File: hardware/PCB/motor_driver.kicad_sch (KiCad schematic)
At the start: 27 parts, among them U2 TMC2209-LA, U3 TB6612FNG, U4 TB6612FNG

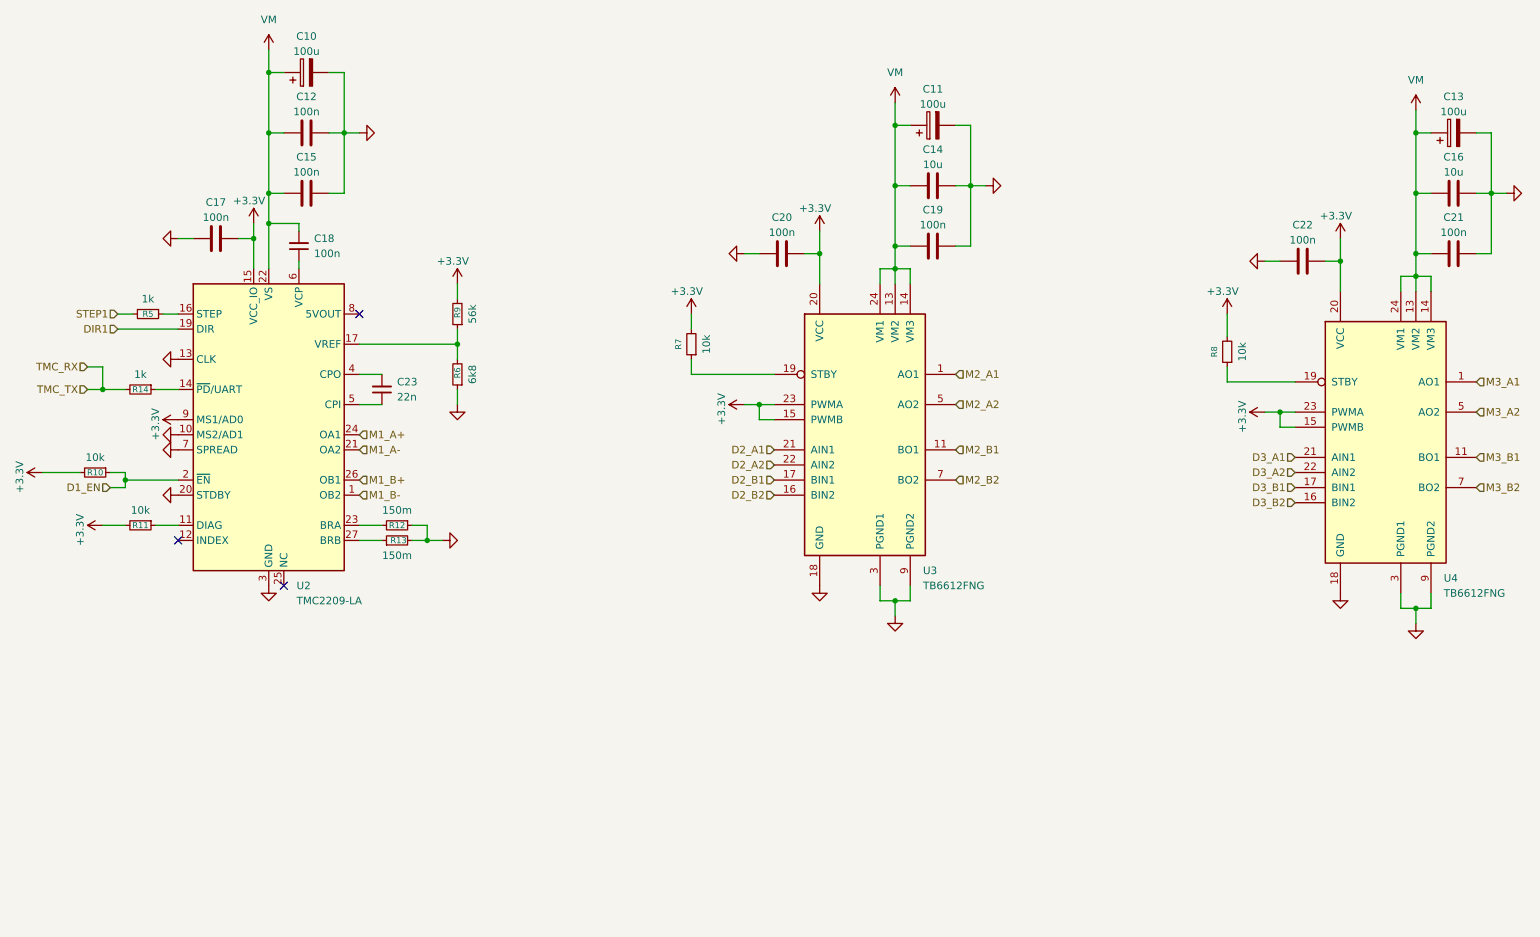
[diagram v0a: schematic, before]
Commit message: Added I2C expander for motor drivers and changed LoRa module
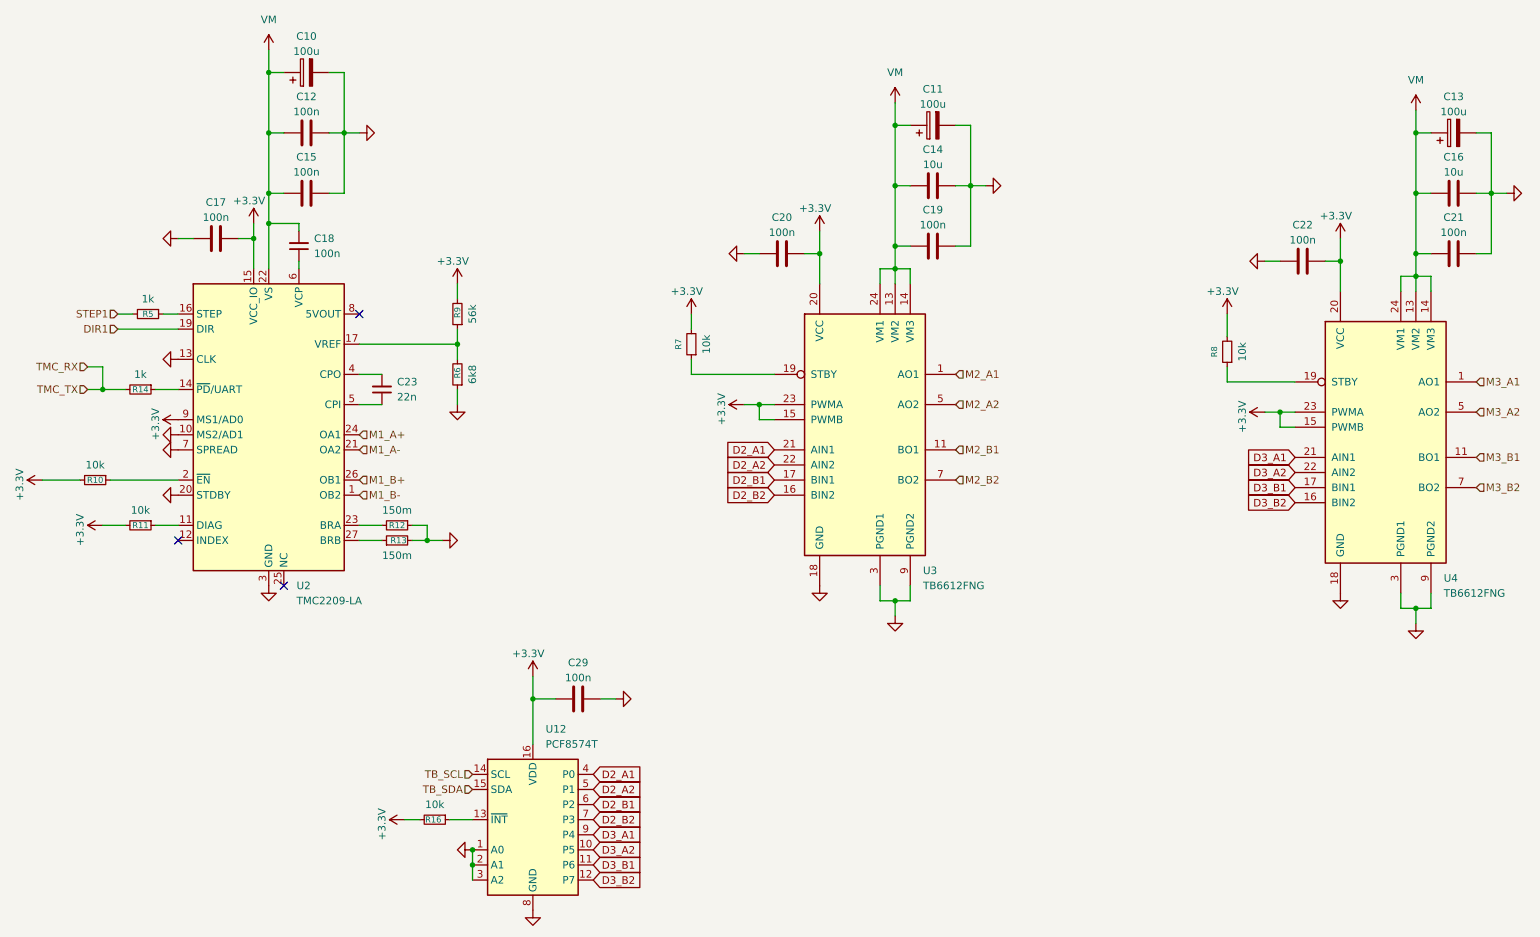
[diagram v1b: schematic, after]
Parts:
- added C29: 100n, Capacitor_SMD:C_1206_3216Metric_Pad1.33x1.80mm_HandSolder, symbol Device:C
- added R16: 10k, Resistor_SMD:R_1206_3216Metric_Pad1.30x1.75mm_HandSolder, symbol Device:R_Small
- added U12: PCF8574T, Package_SO:SOIC-16W_7.5x10.3mm_P1.27mm, symbol Interface_Expansion:PCF8574T
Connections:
- net +3.3V: now also C29.1, R16.2, U12.16 (VDD)
- net D2_A1: now also U12.4 (P0)
- net D2_A2: now also U12.5 (P1)
- net D2_B1: now also U12.6 (P2)
- net D2_B2: now also U12.7 (P3)
- net D3_A1: now also U12.9 (P4)
- net D3_A2: now also U12.10 (P5)
- net D3_B1: now also U12.11 (P6)
- net D3_B2: now also U12.12 (P7)
- net GND: now also C29.2, U12.1 (A0), U12.2 (A1), U12.3 (A2), U12.8 (GND)
- net D1_EN: no longer names the net of R10.1, U2.2 (~{EN})
- new net: R16.1, U12.13 (~{INT})
- new net TB_SCL: U12.14 (SCL)
- new net TB_SDA: U12.15 (SDA)
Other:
- moved on the sheet: R10

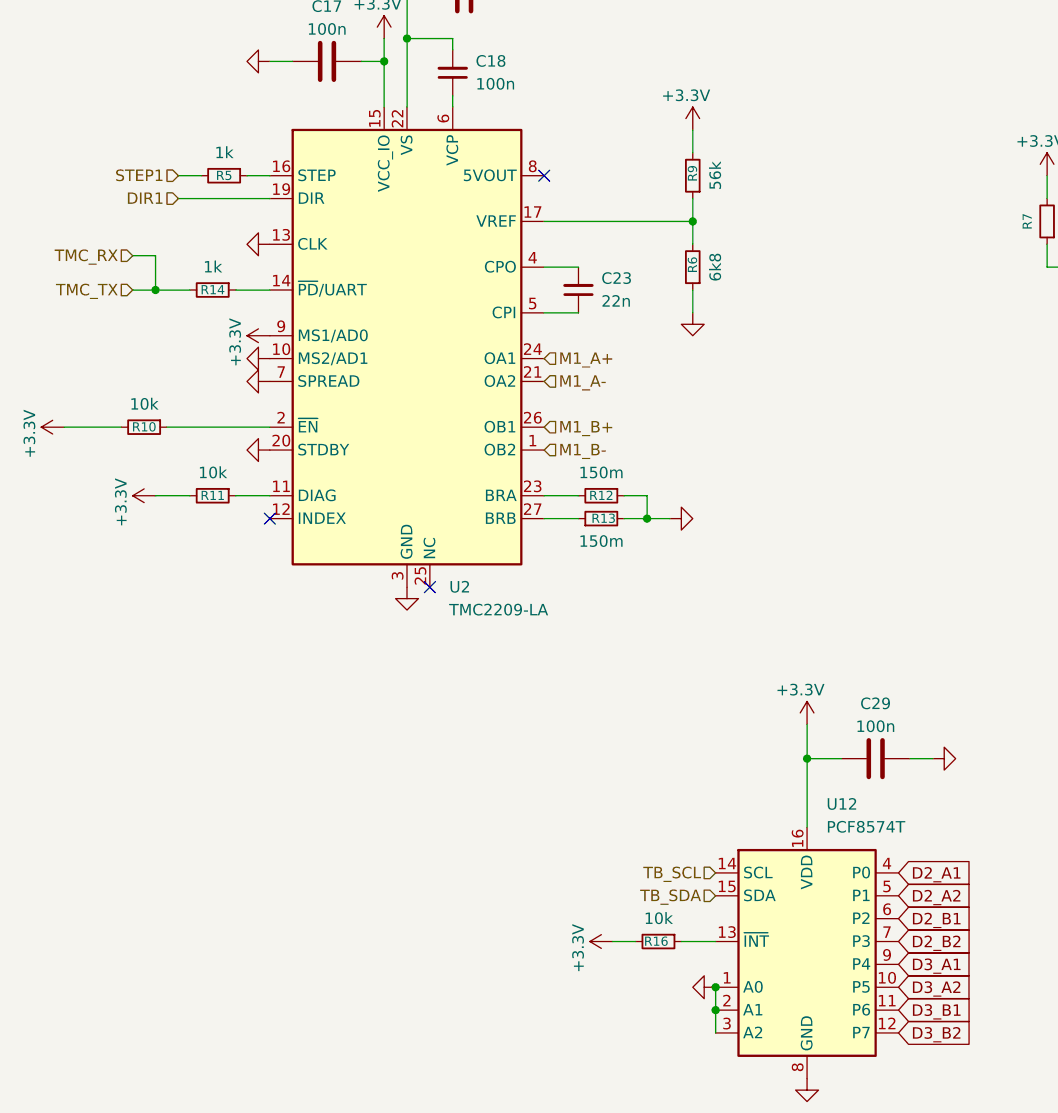
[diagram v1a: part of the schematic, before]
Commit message: Finished schematic for LoRa, added BME280
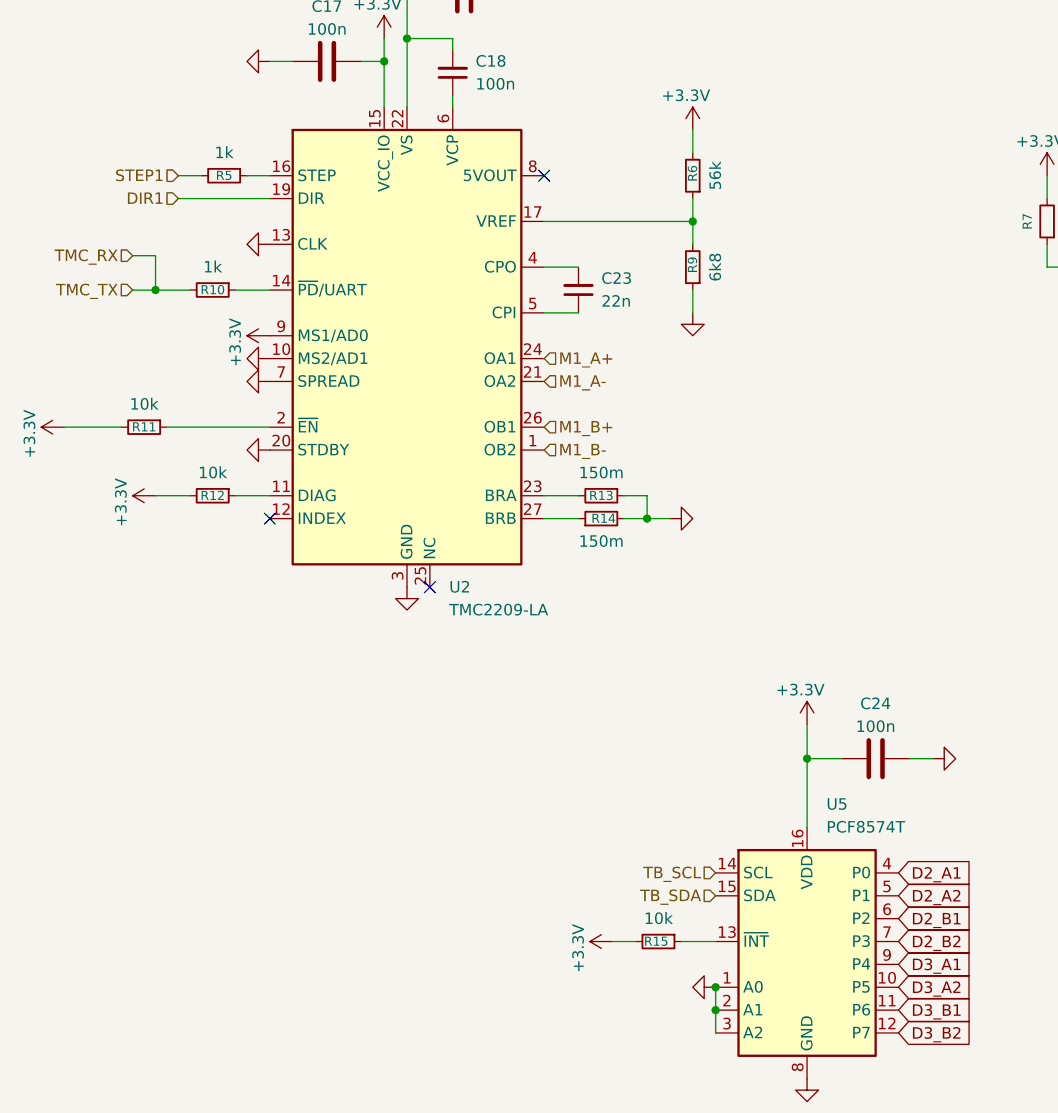
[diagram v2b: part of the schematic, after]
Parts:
- renumbered C29 to C24, R14 to R10, R10 to R11, R11 to R12, R12 to R13, R13 to R14, R16 to R15, R9 to R6, R6 to R9, U12 to U5

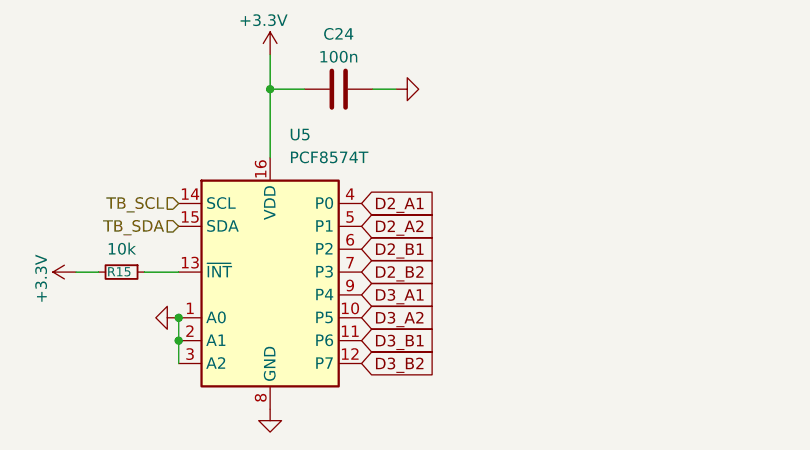
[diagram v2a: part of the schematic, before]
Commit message: Rerouted changes on the PCB layout, Routed LoRa
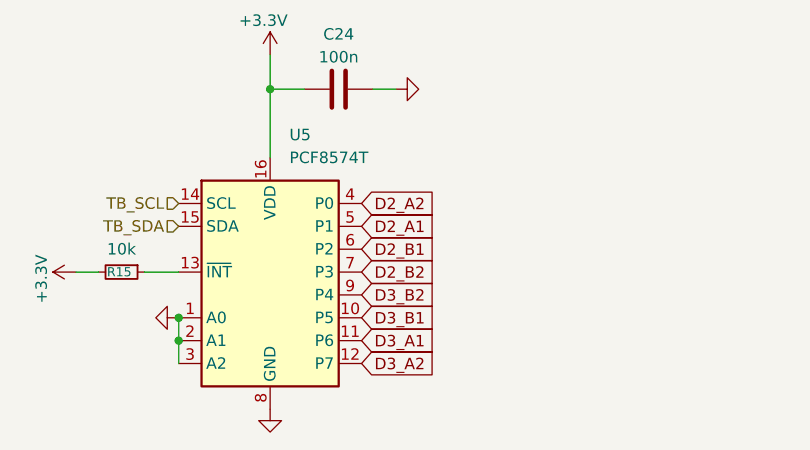
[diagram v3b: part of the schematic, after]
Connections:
- net D2_A1: now also U5.5 (P1); no longer U5.4 (P0)
- net D2_A2: now also U5.4 (P0); no longer U5.5 (P1)
- net D3_A1: now also U5.11 (P6); no longer U5.9 (P4)
- net D3_A2: now also U5.12 (P7); no longer U5.10 (P5)
- net D3_B1: now also U5.10 (P5); no longer U5.11 (P6)
- net D3_B2: now also U5.9 (P4); no longer U5.12 (P7)

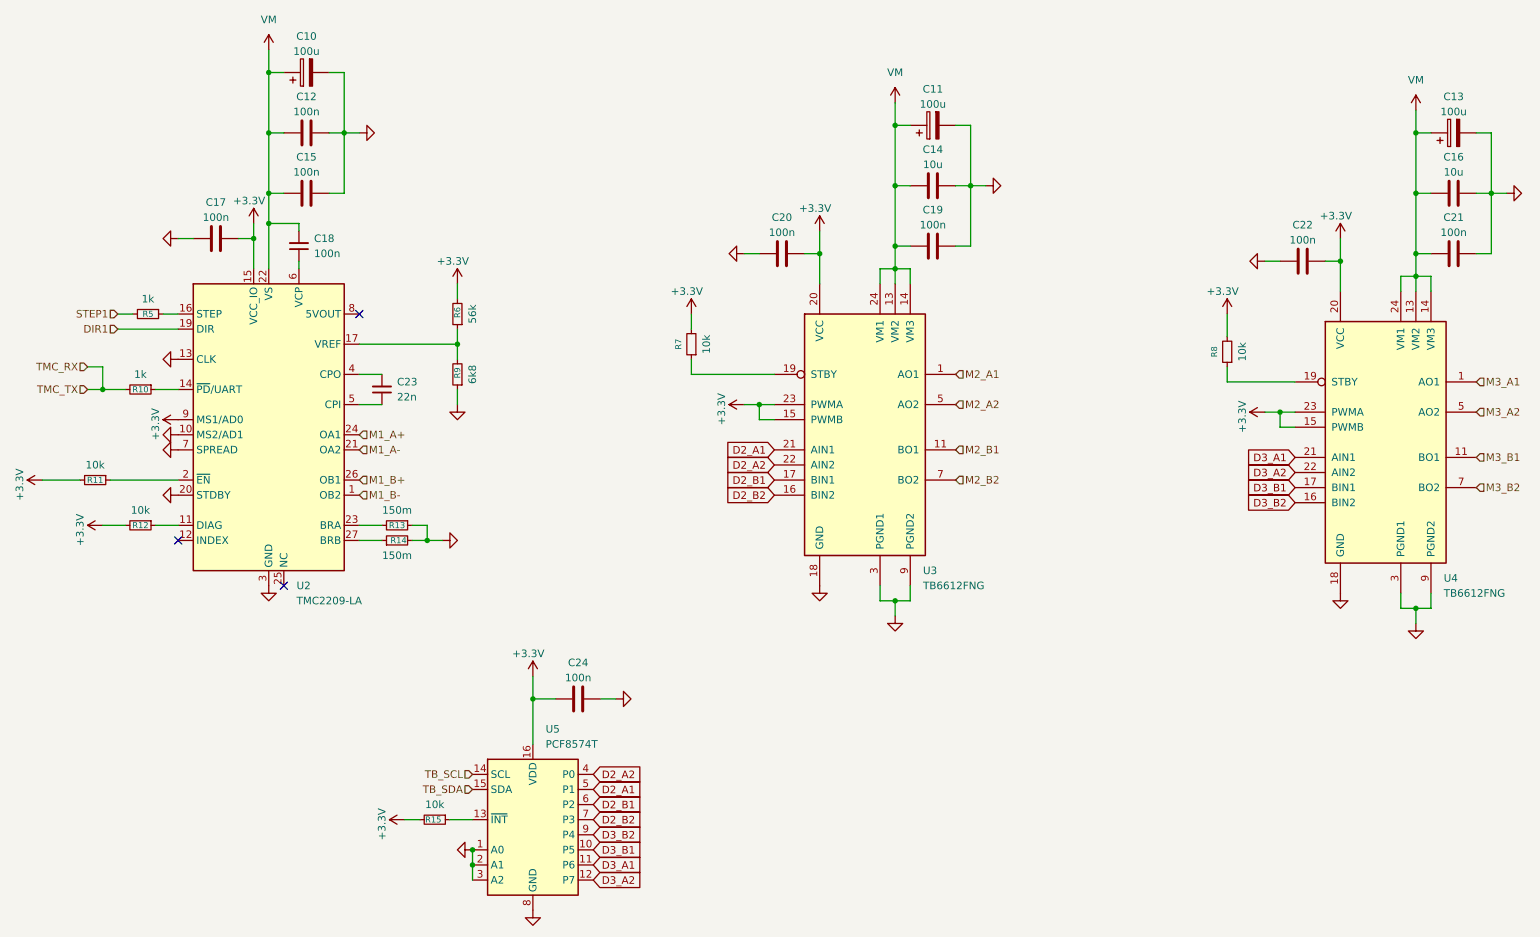
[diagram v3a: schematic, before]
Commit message: Removed polar azimuth motor driver from pcb
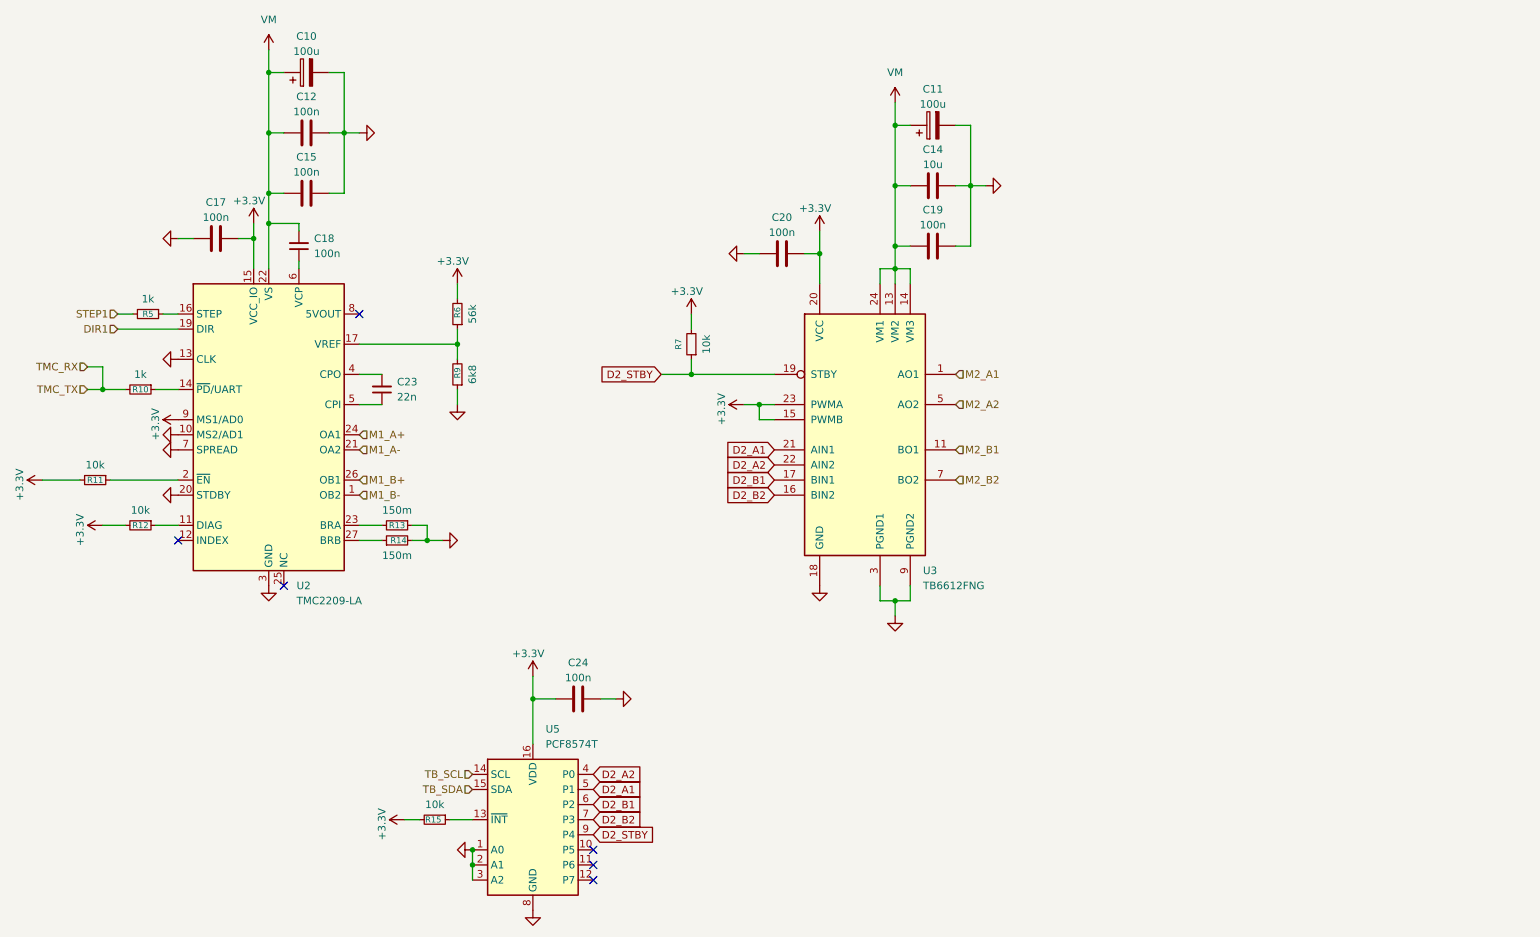
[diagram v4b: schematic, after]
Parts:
- removed C13: 100u, Capacitor_THT:CP_Radial_D5.0mm_P2.00mm, symbol Device:C_Polarized
- removed C16: 10u, Capacitor_SMD:C_1210_3225Metric_Pad1.33x2.70mm_HandSolder, symbol Device:C
- removed C21, C22: 100n, Capacitor_SMD:C_1206_3216Metric_Pad1.33x1.80mm_HandSolder, symbol Device:C
- removed R8: 10k, Resistor_SMD:R_1206_3216Metric_Pad1.30x1.75mm_HandSolder, symbol Device:R_Small
- removed U4: TB6612FNG, Package_SO:SSOP-24_5.3x8.2mm_P0.65mm, symbol Driver_Motor:TB6612FNG
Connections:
- net D3_B2 is gone; now on net D2_STBY: U5.9 (P4)
- net D2_STBY: now reaches R7.1, U3.19 (STBY)
- net D3_A1: no longer names the net of U5.11 (P6)
- net D3_A2: no longer names the net of U5.12 (P7)
- net D3_B1: no longer names the net of U5.10 (P5)
- no-connect marks 3 -> 6
